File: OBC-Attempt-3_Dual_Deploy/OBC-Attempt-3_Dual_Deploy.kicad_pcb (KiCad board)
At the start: 2 copper layers, 25.4 x 25.4 mm, 31 parts, among them J1 Bat, J2 Bat, J3 PWR, J4 DEBUG, J5 CAN Header, SW1 SW_SPDT, SW2 SW_SPST, U1 LD1117S33TR_SOT223, U2 STM32F042G4Ux, U3 SN65HVD230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

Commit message: Re org da files
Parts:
- removed C10: 1uF, Capacitor_SMD:C_0402_1005Metric
- removed C11: 10uF, Capacitor_SMD:C_0402_1005Metric
- removed C12, C13, C14: 100nF, Capacitor_SMD:C_0402_1005Metric
- removed U4: MS560702BA03-50, MS5607:SON125P300X500X100-8N
- removed U5: BMI088, BMI088:PQFN50P450X300X100-16N
- removed U6: MMC5983MA, MMC5983MA:PQFN50P300X300X100-16N
- moved SW2 11.0 mm to (155.9, 118.8), turned to 0 degrees
- moved R1 10.5 mm to (156.5, 112.8), turned to -90 degrees
- moved SW1 10.1 mm to (155.6, 113.8), turned to 180 degrees
- moved R2 9.76 mm to (152.5, 119.3), turned to 180 degrees
- moved C5 9.05 mm to (154.6, 112.8), turned to -90 degrees
- moved U3 9.04 mm to (157.5, 118.6), turned to -90 degrees
- moved C3 8.31 mm to (152.8, 112.8), turned to -90 degrees
- moved C9 7.80 mm to (152.3, 117.7), turned to 0 degrees
- moved X1 7.26 mm to (155.5, 103.5), turned to -90 degrees
- moved C4 7.17 mm to (156.7, 105.7), turned to 0 degrees
- moved R3 5.62 mm to (152.6, 116.1), turned to 0 degrees
- moved U2 5.24 mm to (154.9, 109.2), turned to -90 degrees
- moved C8 4.50 mm to (154.7, 105.7), turned to 180 degrees
- moved C6 2.88 mm to (153.1, 105.5), turned to 90 degrees
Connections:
- U2 pad 10: MAG_INT1 -> unconnected-(U2-Pad10)
- U2 pad 11: SPI1_SCK -> unconnected-(U2-Pad11)
- U2 pad 12: SPI1_MISO -> unconnected-(U2-Pad12)
- U2 pad 13: SPI1_MOSI -> unconnected-(U2-Pad13)
- U2 pad 27: USART1_TX -> unconnected-(U2-Pad27)
- U2 pad 28: USART1_RX -> unconnected-(U2-Pad28)
- U2 pad 6: IMU_INT1 -> unconnected-(U2-Pad6)
- U2 pad 7: IMU_INT2 -> unconnected-(U2-Pad7)
- U2 pad 8: IMU_INT3 -> unconnected-(U2-Pad8)
- U2 pad 9: IMU_INT4 -> unconnected-(U2-Pad9)

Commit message: Work on board
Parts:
- added J6: Conn_01x02_Female, Connector_PinHeader_1.00mm:PinHeader_1x02_P1.00mm_Vertical, F.Cu at (152.7, 122.3)
- added J7: Conn_01x02_Female, Connector_PinHeader_1.00mm:PinHeader_1x02_P1.00mm_Vertical, F.Cu at (157.5, 122.2)
- added R4: 270, Resistor_SMD:R_01005_0402Metric, F.Cu at (152.7, 111.7)
- added R5: 270, Resistor_SMD:R_01005_0402Metric, F.Cu at (153.7, 111.7)
- added U4: CPC1002N, Package_SO:SOP-4_3.8x4.1mm_P2.54mm, F.Cu at (152.3, 117.3)
- added U5: CPC1002N, Package_SO:SOP-4_3.8x4.1mm_P2.54mm, F.Cu at (157.1, 117.3)
- moved C5 8.78 mm to (158.6, 105.0), turned to 0 degrees
- moved U3 8.74 mm to (162.2, 111.2)
- moved C3 8.40 mm to (158.6, 106.8), turned to 0 degrees
- moved R3 8.22 mm to (156.3, 108.7)
- moved R2 8.22 mm to (156.2, 112.0)
- moved C9 8.16 mm to (155.8, 110.3), turned to 180 degrees
- moved J3 7.93 mm to (154.7, 101.2), turned to -90 degrees
- moved X1 7.33 mm to (148.2, 104.4), turned to 0 degrees
- moved C4 6.95 mm to (150.3, 102.9), turned to 90 degrees
- moved SW2 6.28 mm to (159.6, 113.7), turned to -45 degrees
- moved R1 5.82 mm to (152.2, 108.9)
- moved C8 4.41 mm to (150.3, 104.9), turned to -90 degrees
- moved U2 4.40 mm to (154.9, 104.8), turned to 0 degrees
- moved SW1 3.83 mm to (152.2, 111.9)
- moved C6 2.39 mm to (151.0, 106.6), turned to 180 degrees
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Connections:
- U2 pad 8: unconnected-(U2-Pad8) -> Pyro1
- U2 pad 9: unconnected-(U2-Pad9) -> Pyro2
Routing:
- net CAN_RX: track 0.00 -> 20.6 mm
- net +3.3V: track 6.96 -> 26.9 mm, vias 0 -> 2
- net /12V+: track 0.00 -> 16.4 mm
- net CAN_L: track 0.00 -> 14.9 mm
- net GND: track 5.11 -> 18.2 mm, vias 5 -> 17
- net CAN_TX: track 0.00 -> 12.8 mm, vias 0 -> 2
- net CAN_H: track 0.00 -> 9.23 mm, vias 0 -> 1
- net Net-(U5-Pad1): track 0.00 -> 6.55 mm
- net Pyro1: track 0.00 -> 4.99 mm
- net Pyro2: track 0.00 -> 4.76 mm
- net BOOT0: track 0.00 -> 4.24 mm
- net Net-(C9-Pad1): track 0.00 -> 4.04 mm
- net SYS_SWCLK: track 0.00 -> 3.08 mm
- net Net-(R2-Pad1): track 0.00 -> 2.96 mm, vias 0 -> 1
- net Net-(U4-Pad1): track 0.00 -> 2.92 mm
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- added copper zone on F.Cu, net +3.3V
- added copper zone on F.Cu, net /12V+
- added copper zone on F.Cu, net GND

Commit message: futz abt no changes
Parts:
- moved J3 0.11 mm to (154.6, 101.1)
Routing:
- net SYS_SWCLK: track 3.08 -> 0.00 mm
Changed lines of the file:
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@@
     (property "Sheetname" "")
     (attr smd)
-    (fp_text reference "U1" (at -0.25 -4.25 90) (layer "F.SilkS")
+    (fp_text reference "U1" (at 0.05 2.35 90) (layer "F.SilkS")
       (effects (font (size 1 1) (thickness 0.15)))
     )
@@
       (effects (font (size 1 1) (thickness 0.15)))
     )
-    (fp_text user "${REFERENCE}" (at 0 0) (layer "F.Fab")
+    (fp_text user "${REFERENCE}" (at 0 0 90) (layer "F.Fab")
       (effects (font (size 0.8 0.8) (thickness 0.12)))
     )
@@
     (property "Sheetname" "")
     (attr through_hole)
-    (fp_text reference "J4" (at -1.53 0.68) (layer "F.SilkS")
+    (fp_text reference "J4" (at 0.395 -1.47) (layer "F.SilkS")
       (effects (font (size 0.5 0.5) (thickness 0.1)))
     )
@@
   )
   (footprint "Connector_PinHeader_1.00mm:PinHeader_1x02_P1.00mm_Vertical" (layer "F.Cu")
-    (at 154.65 101.17 -90)
+    (at 154.6 101.075 -90)
     (descr "Through hole straight pin header, 1x02, 1.00mm pitch, single row")
     (tags "Through hole pin header THT 1x02 1.00mm single row")
@@
     (property "Sheetname" "")
     (attr through_hole)
-    (fp_text reference "J3" (at 0.08 2.54) (layer "F.SilkS")
+    (fp_text reference "J3" (at 0.025 2.1) (layer "F.SilkS")
       (effects (font (size 0.5 0.5) (thickness 0.1)))
     )
@@
     (property "Sheetname" "")
     (attr smd)
-    (fp_text reference "U2" (at 1.96 -2.95) (layer "F.SilkS")
+    (fp_text reference "U2" (at 1.31 -3.025) (layer "F.SilkS")
       (effects (font (size 0.5 0.5) (thickness 0.1)))
     )
@@
   (segment (start 158.38 102.93) (end 158.06 103.25) (width 0.3) (layer "F.Cu") (net 16))
   (segment (start 158.06 103.25) (end 156.9375 103.25) (width 0.3) (layer "F.Cu") (net 16))
-  (segment (start 154.65 101.17) (end 155.94 101.17) (width 0.3) (layer "F.Cu") (net 17))
-  (segment (start 156.44 101.67) (end 156.44 102.7525) (width 0.3) (layer "F.Cu") (net 17))
-  (segment (start 155.94 101.17) (end 156.44 101.67) (width 0.3) (layer "F.Cu") (net 17))
   (segment (start 155.8 120.03) (end 155.8 118.8) (width 0.5) (layer "F.Cu") (net 20))
   (segment (start 155.3 118.3) (end 150.55 118.3) (width 0.5) (layer "F.Cu") (net 20))

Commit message: AHHHHHHHH
Have to redo all of the footprints haha
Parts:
- R4, R5: footprint Resistor_SMD:R_01005_0402Metric -> Resistor_SMD:R_0402_1005Metric
- moved R4 0.67 mm to (152.1, 112.0)
- moved R5 0.45 mm to (153.7, 112.1)
- moved J3 0.24 mm to (154.4, 101.2)
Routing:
- net +3.3V: track 26.9 -> 31.1 mm, vias 2 -> 3
- net SYS_SWCLK: track 0.00 -> 3.28 mm
- net Net-(U5-Pad1): track 6.55 -> 5.95 mm
- net Pyro1: track 4.99 -> 5.54 mm

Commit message: Cherry Rework
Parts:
- removed J7: Conn_01x02_Female, Connector_PinHeader_1.00mm:PinHeader_1x02_P1.00mm_Vertical
- J6: value Conn_01x02_Female -> Conn_01x03_Female; footprint Connector_PinHeader_1.00mm:PinHeader_1x02_P1.00mm_Vertical -> Connector_PinSocket_2.54mm:PinSocket_1x03_P2.54mm_Vertical
- moved J6 3.99 mm to (156.7, 122.6)
- moved J4 0.99 mm to (158.6, 103.5), turned to 180 degrees
- moved J3 0.55 mm to (154.9, 101.2)
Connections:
- J6 pad 1: Net-(U4-Pad4) -> Net-(U5-Pad4)
- J6 pad 2: GND -> Net-(U4-Pad4)
- U5 pad 4: Net-(J7-Pad1) -> Net-(U5-Pad4)
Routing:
- net Net-(U5-Pad4): track 0.00 -> 3.68 mm
- net GND: track 18.2 -> 14.8 mm
- net Net-(J7-Pad1): track 2.81 -> 0.00 mm
- net CAN_RX: track 20.6 -> 19.5 mm
- net SYS_SWCLK: track 3.28 -> 2.41 mm

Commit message: Yas
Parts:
- J6: value Conn_01x03_Female -> Deployment
- moved J6 5.08 mm to (151.6, 122.4), turned to 90 degrees
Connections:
- J6 pad 1: Net-(U5-Pad4) -> GND
- J6 pad 3: GND -> Net-(U5-Pad4)
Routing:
- net GND: track 14.8 -> 13.9 mm
- net Net-(U5-Pad4): track 3.68 -> 3.06 mm
- net CAN_TX: track 12.8 -> 12.2 mm

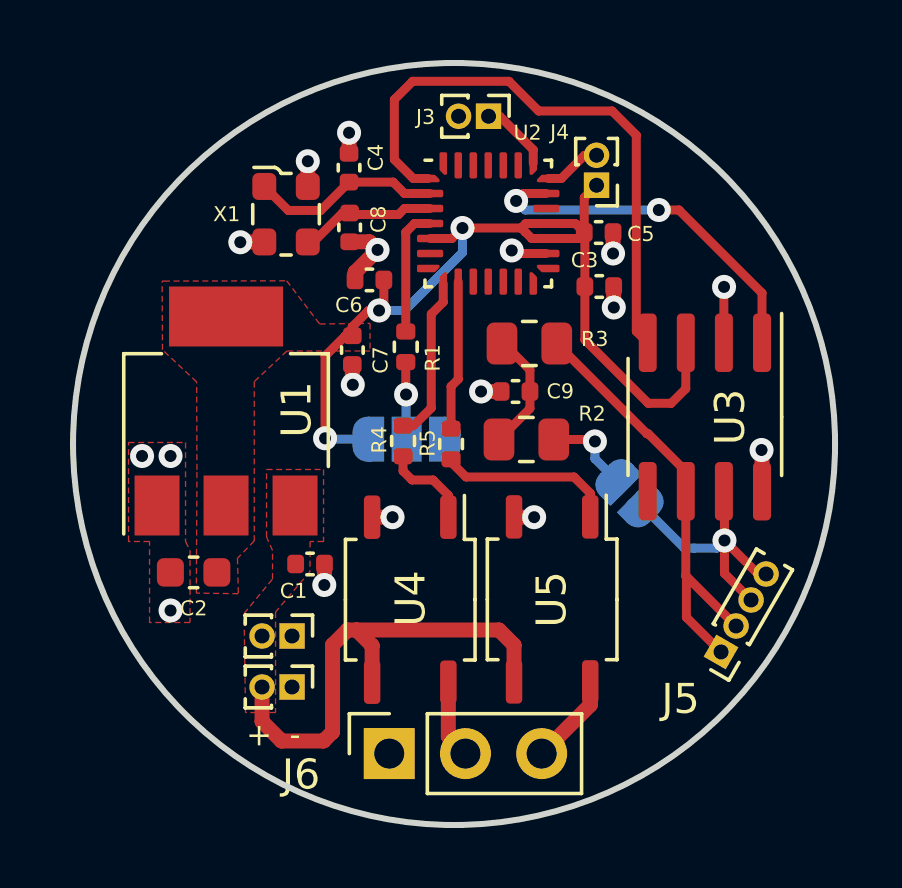
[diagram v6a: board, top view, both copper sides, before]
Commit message: Pad Change
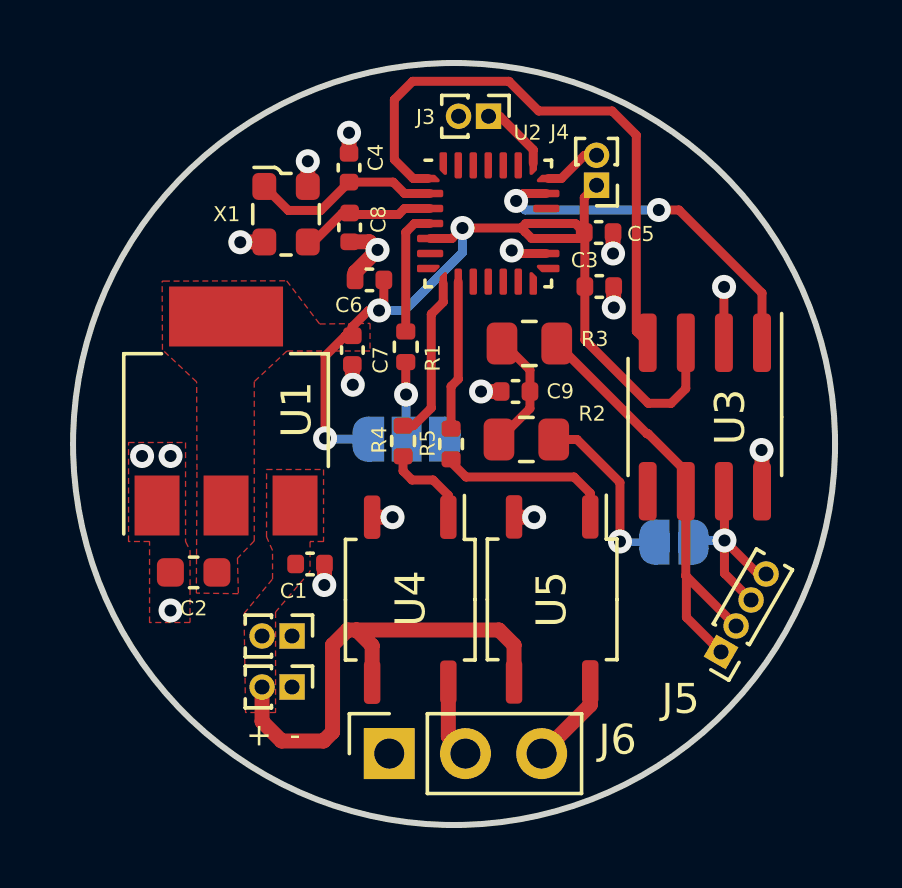
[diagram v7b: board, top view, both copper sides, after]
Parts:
- moved SW2 2.20 mm to (161.1, 115.4), turned to 0 degrees
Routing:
- net Net-(R2-Pad1): track 2.96 -> 5.93 mm
- net CAN_H: track 9.23 -> 6.91 mm
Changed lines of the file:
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@@
     (property "Sheetname" "")
     (attr through_hole)
-    (fp_text reference "J6" (at -0.7 -2.94) (layer "F.SilkS")
+    (fp_text reference "J6" (at 0.46 7.61) (layer "F.SilkS")
       (effects (font (size 1 1) (thickness 0.15)))
     )
@@
   )
   (footprint "Jumper:SolderJumper-2_P1.3mm_Open_RoundedPad1.0x1.5mm" (layer "B.Cu")
-    (at 159.649527 113.741772 -45)
+    (at 161.13 115.37)
     (descr "SMD Solder Jumper, 1x1.5mm, rounded Pads, 0.3mm gap, open")
     (tags "solder jumper open")
@@
     (property "Sheetname" "")
     (attr exclude_from_pos_files)
-    (fp_text reference "SW2" (at 1.491077 1.490408 180) (layer "B.SilkS")
+    (fp_text reference "SW2" (at 1.491077 1.490408 45) (layer "B.SilkS")
       (effects (font (size 0.5 0.5) (thickness 0.1)) (justify mirror))
     )
-    (fp_text value "SW_SPST" (at 0 -1.9 135) (layer "B.Fab") hide
+    (fp_text value "SW_SPST" (at 0 -1.9) (layer "B.Fab") hide
       (effects (font (size 1 1) (thickness 0.15)) (justify mirror))
     )
@@
     (fp_line (start 0.7 -1) (end -0.7 -1) (layer "B.SilkS") (width 0.12))
     (fp_arc (start -0.7 1) (mid -1.194975 0.794975) (end -1.4 0.3) (layer "B.SilkS") (width 0.12))
-    (fp_arc (start 0.7 -1) (mid 1.194974 -0.794975) (end 1.4 -0.3) (layer "B.SilkS") (width 0.12))
+    (fp_arc (start 0.7 -1) (mid 1.194975 -0.794975) (end 1.4 -0.3) (layer "B.SilkS") (width 0.12))
     (fp_arc (start -1.4 -0.3) (mid -1.194975 -0.794975) (end -0.7 -1) (layer "B.SilkS") (width 0.12))
-    (fp_arc (start 1.4 0.3) (mid 1.194975 0.794974) (end 0.7 1) (layer "B.SilkS") (width 0.12))
+    (fp_arc (start 1.4 0.3) (mid 1.194975 0.794975) (end 0.7 1) (layer "B.SilkS") (width 0.12))
     (fp_line (start -1.65 1.25) (end -1.65 -1.25) (layer "B.CrtYd") (width 0.05))
     (fp_line (start -1.65 1.25) (end 1.65 1.25) (layer "B.CrtYd") (width 0.05))
     (fp_line (start 1.65 -1.25) (end 1.65 1.25) (layer "B.CrtYd") (width 0.05))
     (fp_line (start 1.65 -1.25) (end -1.65 -1.25) (layer "B.CrtYd") (width 0.05))
-    (pad "1" smd custom (at -0.65 0 315) (size 1 0.5) (layers "B.Cu" "B.Mask")
+    (pad "1" smd custom (at -0.65 0) (size 1 0.5) (layers "B.Cu" "B.Mask")
       (net 7 "Net-(R2-Pad1)") (pinfunction "A") (pintype "passive") (zone_connect 2)
       (options (clearance outline) (anchor rect))
@@
           ) (width 0) (fill yes))
       ))
-    (pad "2" smd custom (at 0.65 0 315) (size 1 0.5) (layers "B.Cu" "B.Mask")
+    (pad "2" smd custom (at 0.65 0) (size 1 0.5) (layers "B.Cu" "B.Mask")
       (net 8 "CAN_H") (pinfunction "B") (pintype "passive") (zone_connect 2)
       (options (clearance outline) (anchor rect))
@@
   (segment (start 152.2 110.45) (end 152.2 111.92) (width 0.3) (layer "B.Cu") (net 6))
   (segment (start 152.2 111.92) (end 152.22 111.94) (width 0.3) (layer "B.Cu") (net 6))
-  (segment (start 157.1225 111.95) (end 158.432 111.95) (width 0.3) (layer "F.Cu") (net 7))
-  (segment (start 158.432 111.95) (end 158.496 112.014) (width 0.3) (layer "F.Cu") (net 7))
-  (via (at 158.496 112.014) (size 0.8) (drill 0.4) (layers "F.Cu" "B.Cu") (net 7))
-  (segment (start 158.496 112.588245) (end 159.189908 113.282153) (width 0.3) (layer "B.Cu") (net 7))
-  (segment (start 158.496 112.014) (end 158.496 112.588245) (width 0.3) (layer "B.Cu") (net 7))
+  (segment (start 159.33 113.38) (end 159.33 115.35) (width 0.3) (layer "F.Cu") (net 7))
+  (segment (start 157.9 111.95) (end 157.1225 111.95) (width 0.3) (layer "F.Cu") (net 7))
+  (segment (start 157.9 111.95) (end 159.33 113.38) (width 0.3) (layer "F.Cu") (net 7))
+  (via (at 159.33 115.35) (size 0.8) (drill 0.4) (layers "F.Cu" "B.Cu") (net 7))
+  (segment (start 160.48 115.37) (end 159.35 115.37) (width 0.25) (layer "B.Cu") (net 7))
+  (segment (start 159.35 115.37) (end 159.33 115.35) (width 0.25) (layer "B.Cu") (net 7))
   (segment (start 163.931975 116.433975) (end 162.814 115.316) (width 0.3) (layer "F.Cu") (net 8))
   (segment (start 163.7 117.3) (end 162.814 116.414) (width 0.3) (layer "F.Cu") (net 8))
@@
   (segment (start 164.2 116.433975) (end 163.931975 116.433975) (width 0.3) (layer "F.Cu") (net 8))
   (via (at 162.814 115.316) (size 0.8) (drill 0.4) (layers "F.Cu" "B.Cu") (net 8))
-  (segment (start 162.56 115.57) (end 162.814 115.316) (width 0.3) (layer "B.Cu") (net 8))
-  (segment (start 161.798 115.57) (end 162.56 115.57) (width 0.3) (layer "B.Cu") (net 8))
-  (segment (start 161.477755 115.57) (end 161.798 115.57) (width 0.3) (layer "B.Cu") (net 8))
-  (segment (start 160.109146 114.201391) (end 161.477755 115.57) (width 0.3) (layer "B.Cu") (net 8))
+  (segment (start 161.834 115.316) (end 161.78 115.37) (width 0.3) (layer "B.Cu") (net 8))
+  (segment (start 162.814 115.316) (end 161.834 115.316) (width 0.3) (layer "B.Cu") (net 8))
   (segment (start 160.625 104.3) (end 161.297179 104.3) (width 0.3) (layer "F.Cu") (net 9))
   (segment (start 155.868345 103.997521) (end 156.115866 103.75) (width 0.3) (layer "F.Cu") (net 9))
